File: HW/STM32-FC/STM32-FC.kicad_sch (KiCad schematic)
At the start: 52 parts, among them J1 USB_B_Micro, J3 Molex 53048-03, J5 2.54mm Male, J6 2.54mm Male, J8 PWM_Conn_3x08, Q2 S9013, U2 USBLC6-2SC6, U3 AMS1117-3.3, U4 W25X40CLSN, U9 STM32F407VETx, Y1 16MHz

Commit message: 250102:STM32F407VET
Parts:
- removed D2: B5819W, Diode_SMD:D_SOD-123, symbol Device:D_Schottky_Small
- removed J3: Molex 53048-03, Connector_Molex:Molex_PicoBlade_53048-0310_1x03_P1.25mm_Horizontal, symbol Connector_Generic:Conn_01x03
- added D8: B5819W, Diode_SMD:D_SOD-123, symbol Device:D_Schottky_Small
- added J14: USB_C_Receptacle_USB2.0_14P, symbol Connector:USB_C_Receptacle_USB2.0_14P
- added R15: 5.1K, symbol Device:R_US
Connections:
- net +5V: now also D8.1 (K)
- net ACC_NSS: now also U9.3 (PE4); no longer U9.36 (PB1)
- net BARO_NSS: now also U9.5 (PE6); no longer U9.89 (PB3)
- net GND: now also J14.A1 (GND), J14.A12 (GND), J14.B1 (GND), J14.B12 (GND), J14.B5 (CC2), R15.2
- net GYRO_NSS: now also U9.2 (PE3); no longer U9.35 (PB0)
- net LED_BLUE: now also U9.1 (PE2); no longer U9.17 (PC2)
- net LED_GREEN: now also U9.98 (PE1); no longer U9.16 (PC1)
- net LED_RED: now also U9.97 (PE0); no longer U9.15 (PC0)
- net MAG_NSS: now also U9.4 (PE5); no longer U9.37 (PB2)
- net RSSI_IN: now also U9.15 (PC0); no longer U9.34 (PC5)
- net TIM3_CH4: no longer U9.66 (PC9)
- net USB_CONN_D+: now also J14.A6 (D+), J14.B6 (D+)
- net USB_CONN_D-: now also J14.A7 (D-), J14.B7 (D-)
- net VBUS: now also D8.2 (A), J14.A4 (VBUS), J14.A9 (VBUS), J14.B4 (VBUS), J14.B9 (VBUS)
- net V_BATT: now also U9.16 (PC1); no longer U9.33 (PC4)
- net I2C2_SCL: now reaches U9.47 (PB10)
- net I2C2_SDA: now reaches U9.48 (PB11)
- net UART3_TX: now reaches U9.55 (PD8)
- net UART3_RX: now reaches U9.56 (PD9)
- net UART3_CTS: now reaches U9.58 (PD11)
- net UART3_RTS: now reaches U9.59 (PD12)
- net I2C3_SCL: now reaches U9.67 (PA8)
- net UART5_TX: now reaches U9.80 (PC12)
- net UART5_RX: now reaches U9.83 (PD2)
- net UART2_CTS: now reaches U9.84 (PD3)
- net UART2_RTS: now reaches U9.85 (PD4)
- net UART2_TX: now reaches U9.86 (PD5)
- net UART2_RX: now reaches U9.87 (PD6)
- net I2C1_SCL: now reaches U9.95 (PB8)
- net I2C1_SDA: now reaches U9.96 (PB9)
- new net: J14.A5 (CC1), R15.1
- new net I2C3_SDA: U9.66 (PC9)
- no-connect marks 23 -> 17
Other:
- added sheet GPS (io_GPS.kicad_sch)
- added sheet UART (io_UART.kicad_sch)
- note added: "Tele 1"
- note added: "Tele 2"
- moved on the sheet: J8, JP1

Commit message: RC IN modified
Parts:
- removed J5: 2.54mm Male, Connector_PinHeader_2.54mm:PinHeader_1x02_P2.54mm_Vertical, symbol Connector_Generic:Conn_01x02
- removed R4: 10k, Resistor_SMD:R_0402_1005Metric, symbol Device:R_Small_US
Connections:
- net TIM3_CH4: now also J8.6 (CH6), U9.36 (PB1); no longer R13.1
- net TIM3_CH3: now reaches U9.35 (PB0)
- net TIM3_CH3: now also J8.5 (CH5)
- net TIM4_CH2: now reaches U9.60 (PD13)
- net TIM4_CH2: now also J8.8 (CH8), U9.93 (PB7)
- net TIM4_CH3: now reaches U9.61 (PD14)
- net TIM4_CH3: now also R13.1
- net UART1_TX: now reaches U9.68 (PA9)
- net SPI3_SCK: now reaches U9.89 (PB3)
- net SPI3_MISO: now reaches U9.90 (PB4)
- net SPI3_MOSI: now reaches U9.91 (PB5)
- net TIM4_CH1: now reaches U9.92 (PB6)
- net TIM4_CH1: now also J8.7 (CH7)
- no-connect marks 17 -> 13
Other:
- sheet RC_INPUT ports: added PPM_IN, RSSI_IN, UART1_TX; removed none
- note removed: "UART1_TX (NC)"
- moved on the sheet: D8, J14, R15

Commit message: Big Update:IMU/RC/Conn./MCU
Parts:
- removed C13, C15: 10uF, Capacitor_SMD:C_0402_1005Metric, symbol Device:C_Small
- removed C14, C16: 100nF, Capacitor_SMD:C_0402_1005Metric, symbol Device:C_Small
- removed D1, D7, D8: B5819W, Diode_SMD:D_SOD-123, symbol Device:D_Schottky_Small
- removed D3: Red, LED_SMD:LED_0603_1608Metric, symbol Device:LED_Small
- removed D6: Blue, LED_SMD:LED_0603_1608Metric, symbol Device:LED_Small
- removed J1: USB_B_Micro, Connector_USB:USB_Micro-B_Molex-105017-0001, symbol Connector:USB_B_Micro
- removed J14: USB_C_Receptacle_USB2.0_14P, symbol Connector:USB_C_Receptacle_USB2.0_14P
- removed JP1: Jumper, Jumper:SolderJumper-2_P1.3mm_Open_TrianglePad1.0x1.5mm, symbol Jumper:SolderJumper_2_Open
- removed Q2: S9013, digikey-footprints:SOT-23-3, symbol Device:Q_NPN_BEC
- removed R11, R12, R8: 1k, Resistor_SMD:R_0402_1005Metric, symbol Device:R_Small_US
- removed R13: 180, Resistor_SMD:R_0402_1005Metric, symbol Device:R_Small_US
- removed R15: 5.1K, symbol Device:R_US
- removed TP1, TP2, TP3: TestPoint, TestPoint:TestPoint_Pad_D1.0mm, symbol Connector:TestPoint
- removed U2: USBLC6-2SC6, Package_TO_SOT_SMD:SOT-23-6, symbol Power_Protection:USBLC6-2SC6
- removed U3: AMS1117-3.3, Package_TO_SOT_SMD:SOT-223-3_TabPin2, symbol Regulator_Linear:AMS1117-3.3
- removed U4: W25X40CLSN, Package_SO:SOIC-8_3.9x4.9mm_P1.27mm, symbol Memory_Flash:W25X40CLSN
- added D1, D2: Red, LED_SMD:LED_0603_1608Metric, symbol Device:LED_Small
- added D3: B5819W, Diode_SMD:D_SOD-123, symbol Device:D_Schottky_Small
- added Q1: S9013, Package_TO_SOT_SMD:SOT-23-3, symbol Device:Q_NPN_BEC
- added R4: 180, Resistor_SMD:R_0402_1005Metric, symbol Device:R_Small_US
- added R5, R6: 1k, Resistor_SMD:R_0402_1005Metric, symbol Device:R_Small_US
- added TP1, TP2, TP3: Test Pin, Connector_PinHeader_2.54mm:PinHeader_1x03_P2.54mm_Vertical, symbol Connector:Conn_01x03_Socket
- D4: value Red -> Green
- D5: value Green -> Blue
- R3: value 1.5k -> 1k
- renumbered C2 to C1, C1 to C2, C4 to C3, C3 to C4, C6 to C5, C7 to C6, C5 to C7, J6 to J1, J8 to J2, U9 to U1
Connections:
- net ACC_NSS is gone; now on net BARO_NSS: U1.3 (PE4)
- net +3.3V: now also D1.2 (A); no longer R3.1
- net +5V: now also D3.1 (K)
- net BARO_NSS: no longer U1.5 (PE6)
- net CAN1_STBY: now also U1.38 (PE7)
- net GND: now also R3.2, Q1.2 (E), R5.2, R6.2
- net LED_BLUE: now also D5.2 (A)
- net LED_GREEN: now also D4.2 (A); no longer D5.2 (A)
- net LED_RED: now also D2.2 (A); no longer D4.2 (A)
- net MAG_NSS: now also U1.5 (PE6); no longer U1.4 (PE5)
- net SPI1_MISO: now also TP2.3 (Pin_3)
- net SPI1_MOSI: now also TP2.2 (Pin_2)
- net SPI1_SCK: now also TP2.1 (Pin_1)
- net SPI2_MISO: now also TP1.3 (Pin_3)
- net SPI2_MOSI: now also TP1.2 (Pin_2)
- net SPI2_SCK: now also TP1.1 (Pin_1)
- net SPI3_MISO: now also TP3.3 (Pin_3)
- net SPI3_MOSI: now also TP3.2 (Pin_2)
- net SPI3_SCK: now also TP3.1 (Pin_1)
- net TIM4_CH3: now also R4.1
- net USB_D+: no longer R3.2
- net at BZ1.2 (+): now also D3.2 (A), Q1.3 (C)
- net at D5.1 (K): now also R7.1
- net at D4.1 (K): now also R6.1
- net GYRO_NSS renamed GYRO1_NSS
- new net: Q1.1 (B), R4.2
- new net: D2.1 (K), R5.1
- new net: D1.1 (K), R3.1
- new net GYRO2_NSS: U1.4 (PE5)
- no-connect marks 13 -> 1
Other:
- removed sheet CAN
- removed sheet UART
- added sheet Communication (io_communication.kicad_sch)
- added sheet Memory (memory.kicad_sch)
- added sheet USB & POWER (usb.kicad_sch)
- sheet Sensors ports: added GYRO1_NSS, GYRO2_NSS, SS2_SPI_MISO, SS2_SPI_MOSI, SS2_SPI_SCK; removed ACC_NSS, GYRO_NSS
- note added: "Memory & SD Card"
- note added: "USB & POWER"
- note removed: "Flash Memory"
- note removed: "Tele 1"
- note removed: "Tele 2"
- note removed: "Test Points"
- note removed: "USB"
- note removed: "Voltage Regulator"
- company: casterian.net -> INHA UNIV. NARAE
- moved on the sheet: C1, C10, C11, C12, C2, C3, C4, C5, C6, C7, C8, C9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

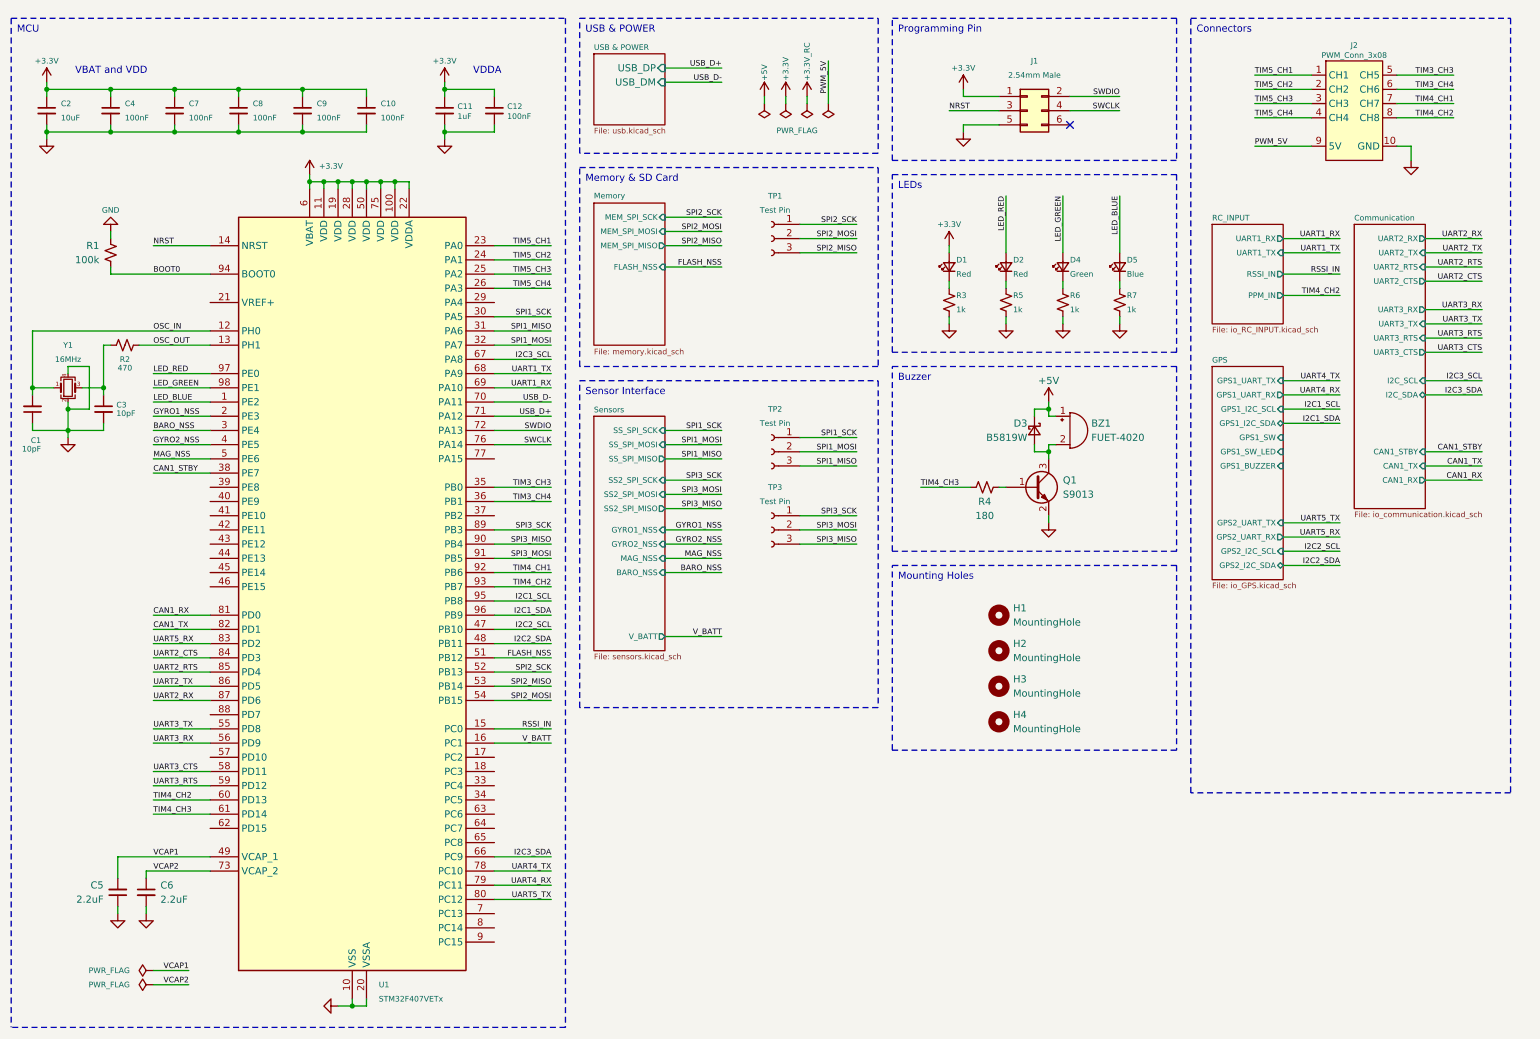
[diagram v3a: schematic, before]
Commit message: 2025.01.03v2:PM(Power Module) added
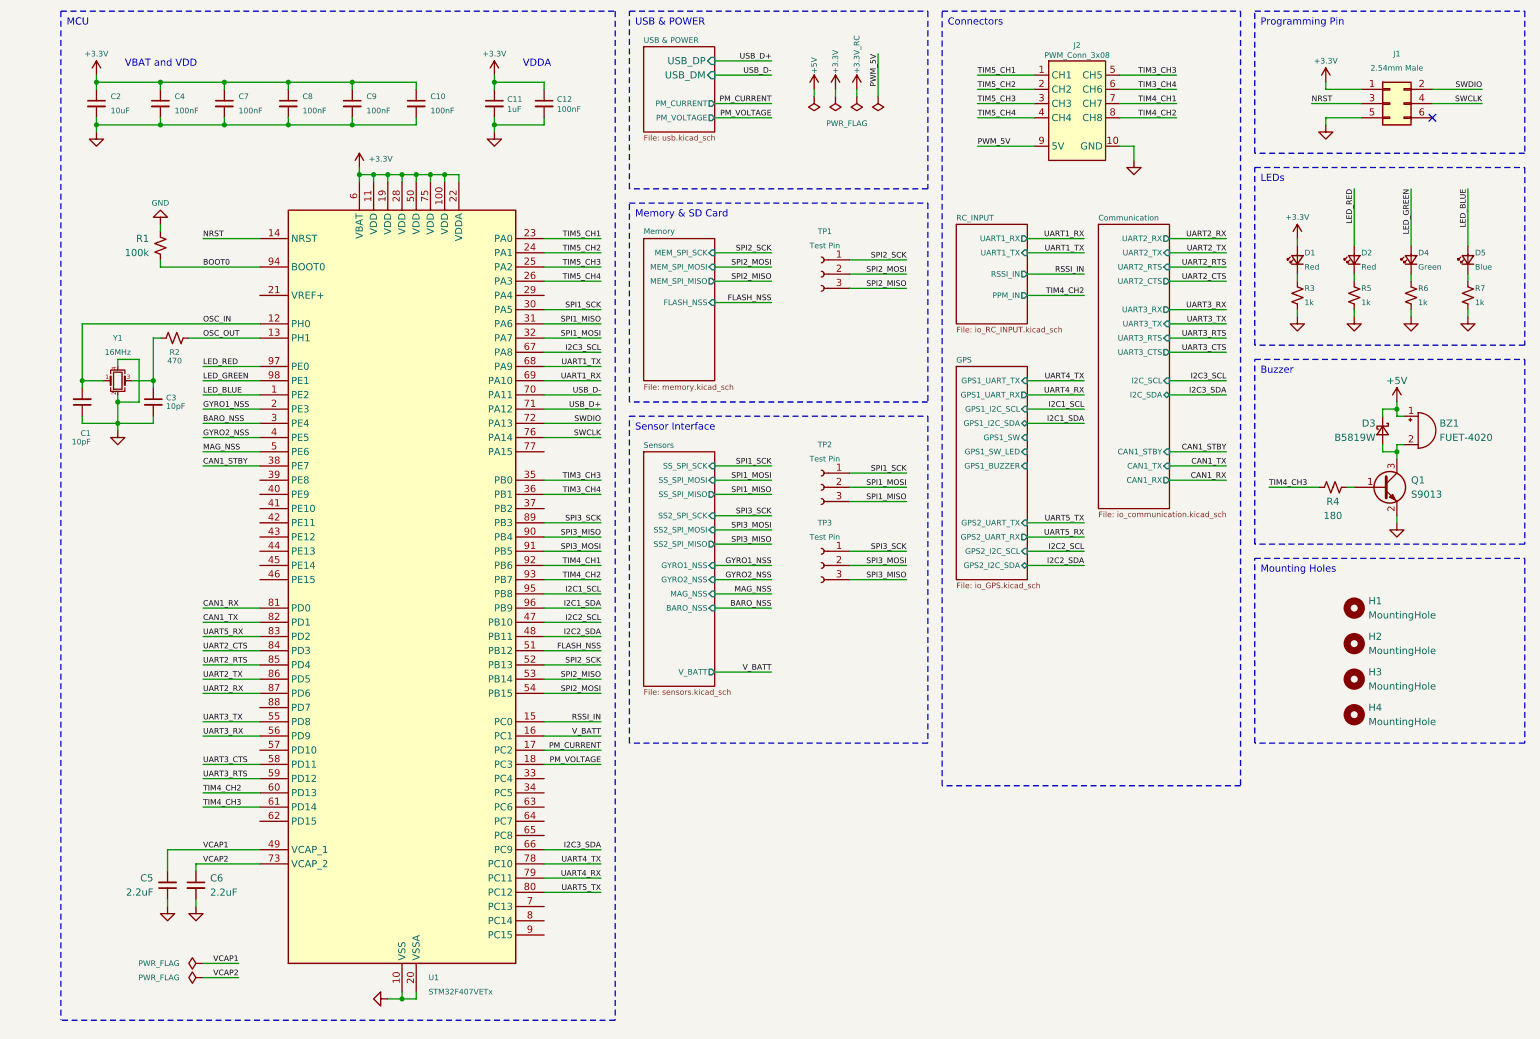
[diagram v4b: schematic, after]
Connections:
- net PM_CURRENT: now reaches U1.17 (PC2)
- net PM_VOLTAGE: now reaches U1.18 (PC3)
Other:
- sheet USB & POWER ports: added PM_CURRENT, PM_VOLTAGE; removed none
- company: INHA UNIV. NARAE -> NARAE
- moved on the sheet: BZ1, C1, C10, C11, C12, C2, C3, C4, C5, C6, C7, C8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

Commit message: Baro/SD Card update
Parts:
- removed J1: 2.54mm Male, Connector_PinHeader_2.54mm:PinHeader_2x03_P2.54mm_Vertical, symbol Connector_Generic:Conn_02x03_Odd_Even
- added J2: PWM_Conn_3x04, PWM_Connector:PWM_Conn_3x04, symbol PWM_Connector:PWM_Conn_3x04
- added J3: GH 1.25mm 6P, JST_GH:JST_GH_BM06B-GHS-TBT_06, symbol Connector_Generic:Conn_01x06
- H1, H2, H3, H4: footprint MountingHole:MountingHole_3.2mm_M3 -> MountingHole:MountingHole_2.7mm_M2.5
- R2: value 470 -> 4k7
- TP1: renamed from TP2; footprint Connector_PinHeader_2.54mm:PinHeader_1x03_P2.54mm_Vertical -> Connector_PinHeader_1.27mm:PinHeader_1x03_P1.27mm_Vertical
- TP2: renamed from TP1; footprint Connector_PinHeader_2.54mm:PinHeader_1x03_P2.54mm_Vertical -> Connector_PinHeader_1.27mm:PinHeader_1x03_P1.27mm_Vertical
- TP3: footprint Connector_PinHeader_2.54mm:PinHeader_1x03_P2.54mm_Vertical -> Connector_PinHeader_1.27mm:PinHeader_1x03_P1.27mm_Vertical
- renumbered J2 to J1
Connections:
- net +3.3V: now also U1.21 (VREF+), J3.1 (Pin_1)
- net CAN1_STBY: now also U1.33 (PC4); no longer U1.38 (PE7)
- net FLASH_NSS: now also U1.7 (PC13); no longer U1.51 (PB12)
- net GND: now also J2.6 (GND), J3.6 (Pin_6)
- net NRST: now also J3.4 (Pin_4)
- net SWCLK: now also J3.3 (Pin_3)
- net SWDIO: now also J3.2 (Pin_2)
- net TIM3_CH3: now also J1.7 (CH7); no longer J1.5 (CH5)
- net TIM3_CH4: now also J1.8 (CH8); no longer J1.6 (CH6)
- net TIM4_CH2: now also J2.1 (CH1); no longer J1.8 (CH8), U1.60 (PD13)
- net CAN2_STBY: now reaches U1.34 (PC5)
- net GPS1_LED: now reaches U1.39 (PE8)
- net GPS1_BUZZER: now reaches U1.40 (PE9)
- net GPS1_LED_SW: now reaches U1.41 (PE10)
- net TIM1_CH2: now reaches U1.42 (PE11)
- net TIM1_CH2: now also J2.2 (CH2)
- net TIM1_CH3: now reaches U1.44 (PE13)
- net TIM1_CH3: now also J2.3 (CH3)
- net TIM1_CH4: now reaches U1.45 (PE14)
- net TIM1_CH4: now also J2.4 (CH4)
- net TIM4_CH4: now reaches U1.62 (PD15)
- net TIM3_CH1: now reaches U1.63 (PC6)
- net TIM3_CH1: now also J1.5 (CH5)
- net TIM3_CH2: now reaches U1.64 (PC7)
- net TIM3_CH2: now also J1.6 (CH6)
- net MSD_NSS: now reaches U1.8 (PC14)
- net MSD_DETECT: now reaches U1.9 (PC15)
- net PWM_5V renamed +5V_PWM
- net +5V_PWM: now also J2.5 (5V)
- net TIM4_CH1 renamed CAN2_TX
- net CAN2_TX: no longer J1.7 (CH7)
- new net BARO_INT: U1.38 (PE7)
- new net CAN2_RX: U1.51 (PB12)
- no-connect marks 1 -> 10
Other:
- sheet Communication ports: added CAN2_RX, CAN2_STBY, CAN2_TX; removed none
- sheet Memory ports: added MSD_DETECT, MSD_NSS; removed none
- sheet Sensors ports: added BARO_INT; removed none
- sheet USB & POWER ports: added USB_D+, USB_D-; removed USB_DM, USB_DP
- moved on the sheet: J1

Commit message: 2025.01.16
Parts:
- D5: renamed from D3; footprint Diode_SMD:D_SOD-123 -> Diode_SMD:D_SOD-323
- H1, H2, H3, H4: footprint MountingHole:MountingHole_2.7mm_M2.5 -> MountingHole:MountingHole_2.2mm_M2
- renumbered C2 to C1, C3 to C10, C5 to C11, C6 to C12, C4 to C2, C7 to C3, C8 to C4, C9 to C5, C10 to C6, C11 to C7, C12 to C8, C1 to C9, D4 to D3, D5 to D4, J3 to J1, J1 to J2, J2 to J3, R5 to R4, R6 to R5, R7 to R6, R4 to R7, TP2 to TP1, TP1 to TP2
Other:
- note added: "M2.5"
- note added: "PA13 : SWDIO PA14 : SWCLK"
- note added: "PD14 : TIM4_CH3"
- note added: "PE0 : R PE1 : G PE2 : B"
- moved on the sheet: BZ1, C10, C9, D1, D2, D3, D4, D5, H1, H2, H3, H4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

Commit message: 2025.01.17 : PCB layout
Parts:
- removed J2: PWM_Conn_3x08, PWM_Connector:PWM_Conn_3x08, symbol PWM_Connector:PWM_Conn_3x08
- removed J3: PWM_Conn_3x04, PWM_Connector:PWM_Conn_3x04, symbol PWM_Connector:PWM_Conn_3x04
- added R2: 100k, Resistor_SMD:R_0402_1005Metric, symbol Device:R_Small_US
- added SW2: SW_DIP_x03, Button_Switch_SMD:SW_DIP_SPSTx03_Slide_KingTek_DSHP03TJ_W5.25mm_P1.27mm_JPin, symbol Switch:SW_DIP_x03
- H1, H2, H3, H4: footprint MountingHole:MountingHole_2.2mm_M2 -> Hole:MountingHole_2.2mm_M2
- renumbered C9 to C1, C6 to C10, C7 to C11, C8 to C12, C1 to C2, C2 to C3, C10 to C4, C11 to C5, C12 to C6, C3 to C7, C4 to C8, C5 to C9, D5 to D3, D3 to D4, D4 to D5, R2 to R3, R3 to R4, R7 to R5, R4 to R6, R5 to R7, R6 to R8
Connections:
- net +3.3V: now also SW2.1, SW2.2
- net +5V: now also SW2.4
- net +5V_PWM: now also SW2.3
- net BOOT0: now also R1.2, SW2.6; no longer R1.1
- net GND: now also R1.1, R2.1; no longer R1.2
- net BOOT1: now reaches U1.77 (PA15)
- net BOOT1: now also R2.2, SW2.5
- no-connect marks 10 -> 9
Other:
- sheet RC_INPUT ports: added AUX_CH1, AUX_CH2, AUX_CH3, AUX_CH4, MAIN_CH1, MAIN_CH2, MAIN_CH3, MAIN_CH4, MAIN_CH5, MAIN_CH6, MAIN_CH7, MAIN_CH8; removed none
- note added: "- Boot |X|0| : Main Flash |0|1| : System FLASH |1|1| : SRAM - PWR Select Switch to set power supplied from BEC to be supplied to the board"
- note added: "Boot & 5V PWR Select"
- note added: "M2"
- note removed: "M2.5"
- moved on the sheet: R1, TP1, TP2, TP3
